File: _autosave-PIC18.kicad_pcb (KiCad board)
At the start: 2 copper layers, 21 parts, among them J1 Conn_02x20_Counter_Clockwise, J2 Conn_01x06, J3 USB_A, J4 Conn_01x03, J5 Conn_01x02, U1 PIC18F4321-I/P, U2 LM4040DBZ-4.1, U3 FT230XS, Y1 8 MHz

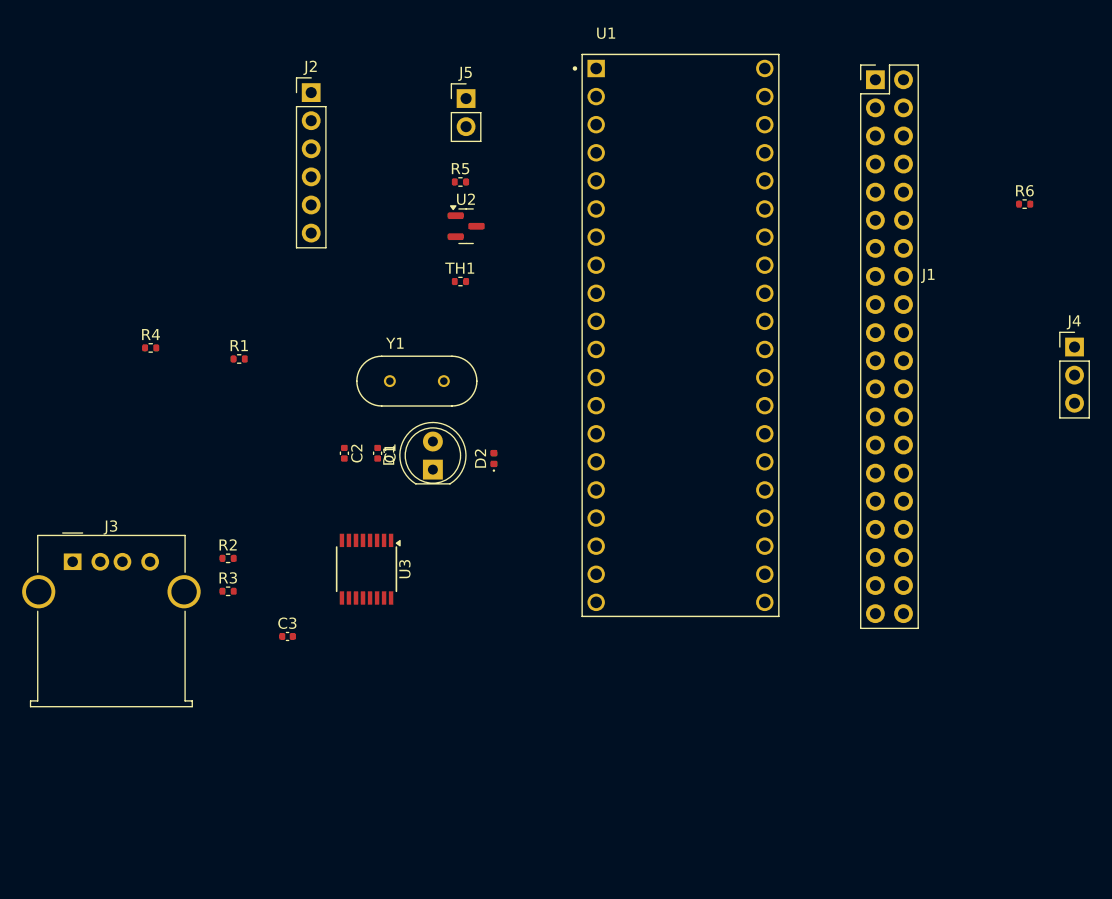
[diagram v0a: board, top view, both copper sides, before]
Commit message: More footprint assignments
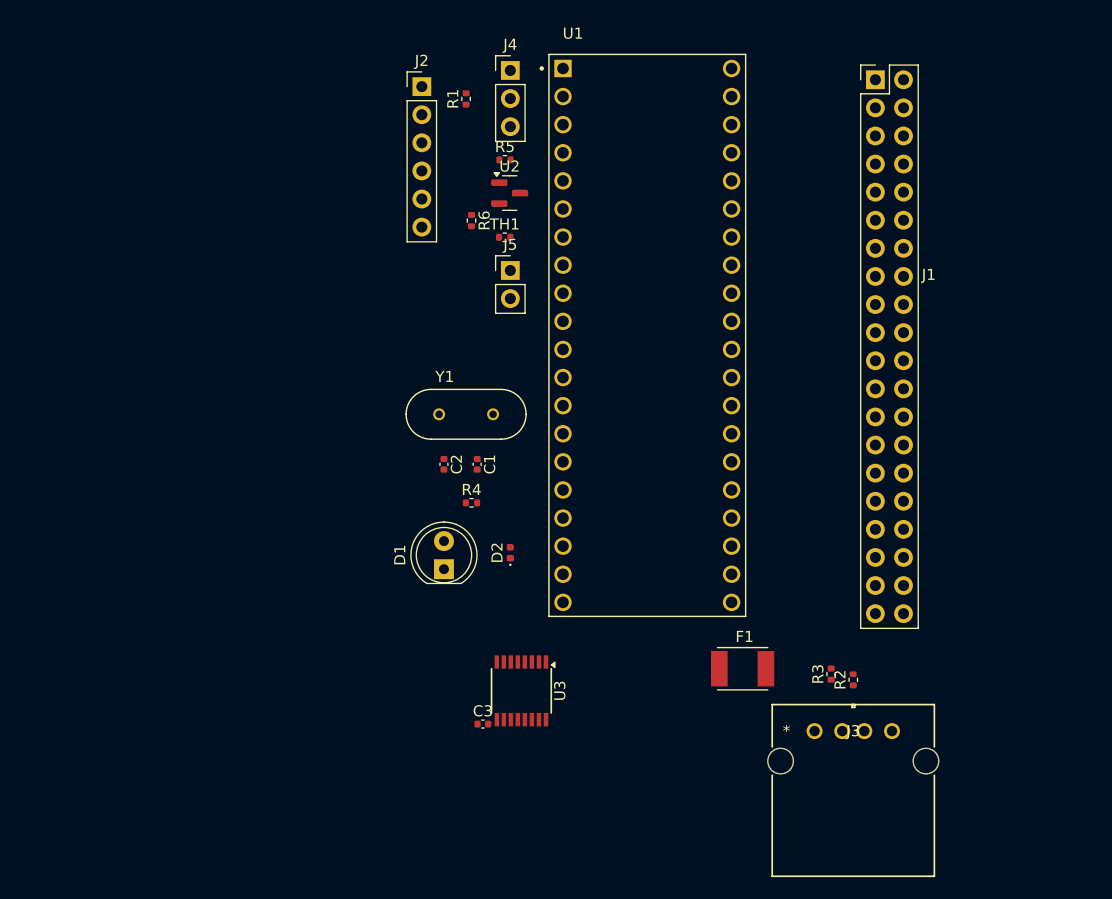
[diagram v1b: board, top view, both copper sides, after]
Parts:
- added F1: MF-MSMF200-2, MF-MSMF200-2:FUSER_MF-MSMF200-2, F.Cu at (188.0, 124.0)
- J3: footprint Connector_USB:USB_A_Molex_67643_Horizontal -> ul_676433910:CONN_67643-3910_MOL
- moved J3 68.8 mm to (194.5, 129.6)
- moved R2 57.6 mm to (198.0, 125.0), turned to 90 degrees
- moved J4 56.8 mm to (167.0, 69.9)
- moved R3 55.0 mm to (196.0, 124.5), turned to 90 degrees
- moved R6 50.0 mm to (163.5, 83.5), turned to -90 degrees
- moved R4 32.2 mm to (163.5, 109.0)
- moved R1 31.2 mm to (163.0, 72.5), turned to 90 degrees
- moved C3 19.4 mm to (164.5, 129.0)
- moved U3 17.8 mm to (168.0, 126.0)
- moved J5 16.0 mm to (167.0, 88.0)
- moved J2 10.0 mm to (159.0, 71.4)
- moved C1 9.06 mm to (164.0, 105.5)
- moved C2 9.06 mm to (161.0, 105.5)
- moved D1 9.06 mm to (161.0, 115.0)
- moved D2 8.64 mm to (167.0, 113.5)
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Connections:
- J3 pad 1: unconnected-(J3-VBUS-Pad1) -> Net-(J3-VBUS)
